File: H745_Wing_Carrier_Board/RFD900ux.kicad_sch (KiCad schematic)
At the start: 1 part

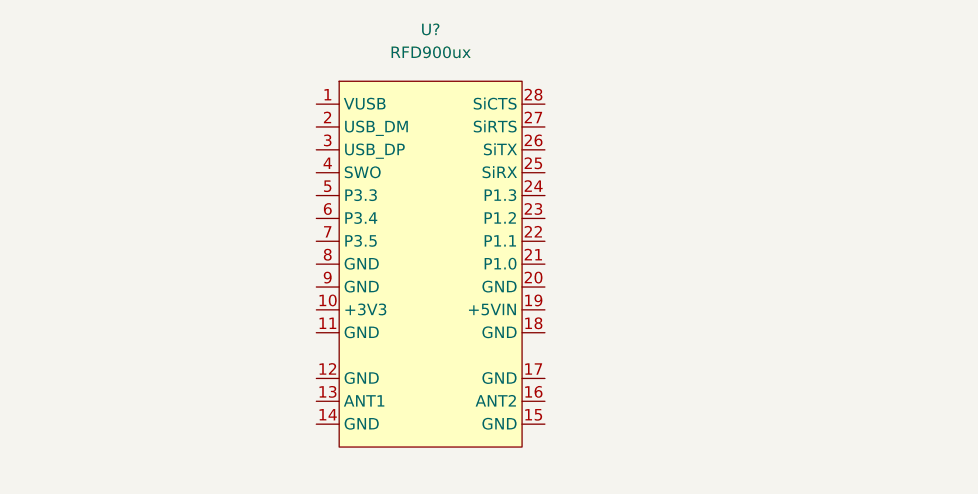
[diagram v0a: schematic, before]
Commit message: Added rfd900ux
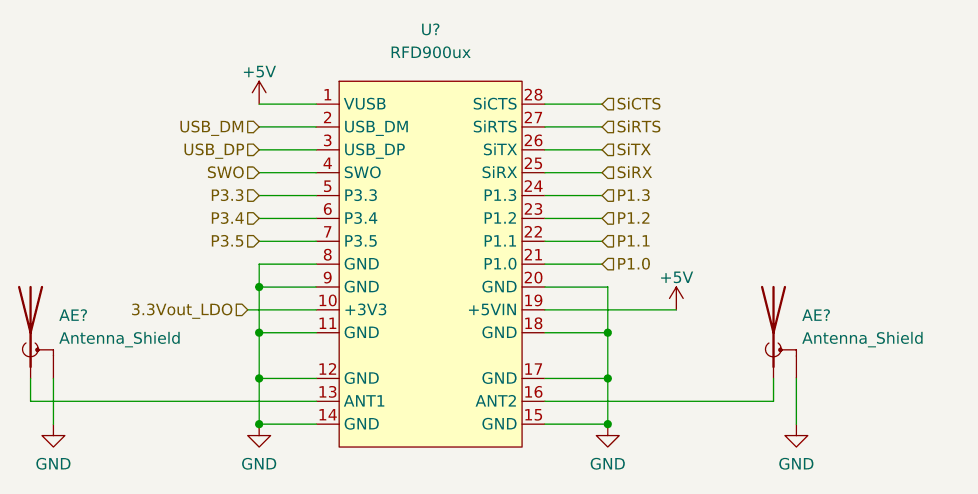
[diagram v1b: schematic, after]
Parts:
- added AE? (x2): Antenna_Shield, symbol Device:Antenna_Shield
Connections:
- net +5V: now reaches U?.1 (VUSB)
- net +5V: now also U?.19 (+5VIN)
- net 3.3Vout_LDO: now reaches U?.10 (+3V3)
- net GND: now reaches U?.11 (GND)
- net GND: now also U?.12 (GND), U?.14 (GND), U?.15 (GND), U?.17 (GND), U?.18 (GND), U?.20 (GND), U?.8 (GND), U?.9 (GND), AE?.2 (Shield), AE?.2 (Shield)
- net at U?.13 (ANT1): now also AE?.1 (A)
- net at U?.16 (ANT2): now also AE?.1 (A)
- net USB_DM: now reaches U?.2 (USB_DM)
- net P1.0: now reaches U?.21 (P1.0)
- net P1.1: now reaches U?.22 (P1.1)
- net P1.2: now reaches U?.23 (P1.2)
- net P1.3: now reaches U?.24 (P1.3)
- net SiRX: now reaches U?.25 (SiRX)
- net SiTX: now reaches U?.26 (SiTX)
- net SiRTS: now reaches U?.27 (SiRTS)
- net SiCTS: now reaches U?.28 (SiCTS)
- net USB_DP: now reaches U?.3 (USB_DP)
- net SWO: now reaches U?.4 (SWO)
- net P3.3: now reaches U?.5 (P3.3)
- net P3.4: now reaches U?.6 (P3.4)
- net P3.5: now reaches U?.7 (P3.5)

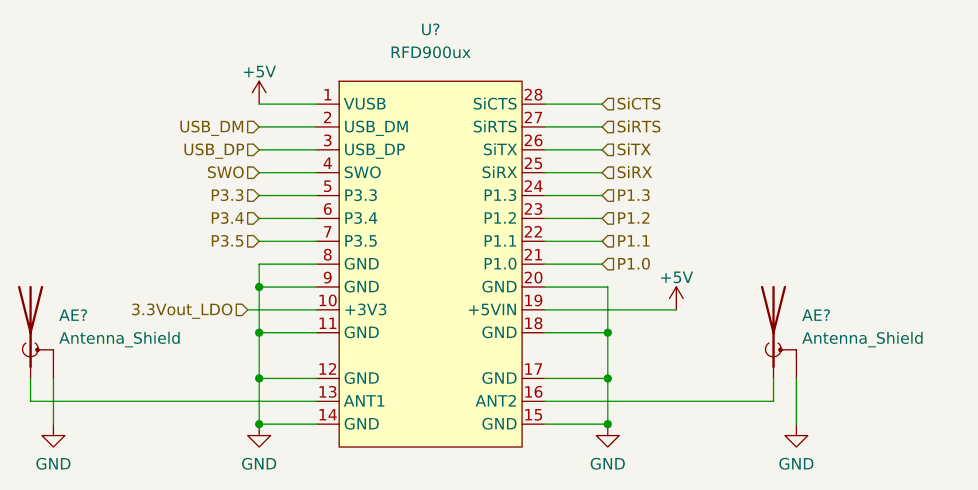
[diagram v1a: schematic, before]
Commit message: Added footprints for ux
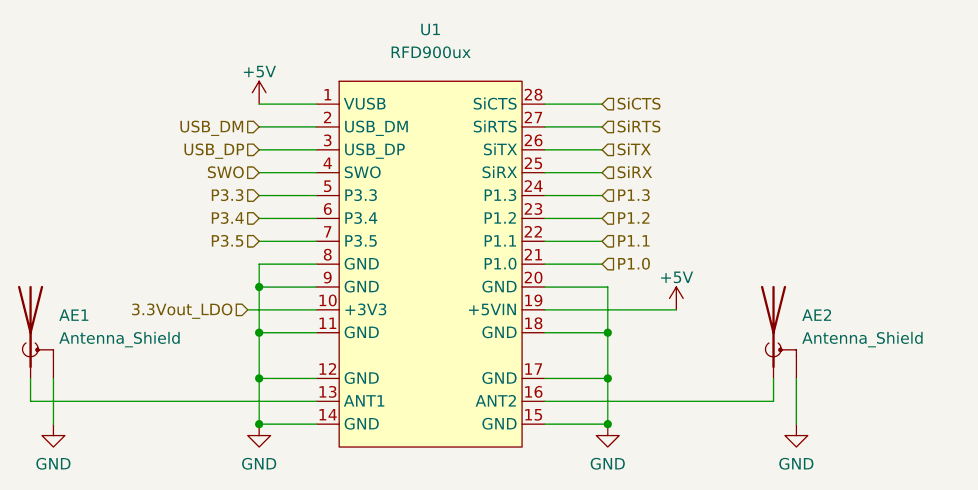
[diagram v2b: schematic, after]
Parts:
- AE1, AE2: renamed from AE?; footprint (none) -> Connector_Coaxial:SMA_Amphenol_132134-16_Vertical
- gave numbers to parts that had none: 1
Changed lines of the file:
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@@
   (symbol (lib_id "power:GND") (at 107.315 111.125 0) (unit 1)
     (in_bom yes) (on_board yes) (fields_autoplaced)
-    (property "Reference" "#PWR?" (id 0) (at 107.315 117.475 0)
+    (property "Reference" "#PWR0108" (id 0) (at 107.315 117.475 0)
       (effects (font (size 1.27 1.27)) hide)
     )
@@
   (symbol (lib_id "power:GND") (at 189.865 111.125 0) (unit 1)
     (in_bom yes) (on_board yes) (fields_autoplaced)
-    (property "Reference" "#PWR?" (id 0) (at 189.865 117.475 0)
+    (property "Reference" "#PWR0110" (id 0) (at 189.865 117.475 0)
       (effects (font (size 1.27 1.27)) hide)
     )
@@
   (symbol (lib_id "Device:Antenna_Shield") (at 104.775 100.965 0) (unit 1)
     (in_bom yes) (on_board yes) (fields_autoplaced)
-    (property "Reference" "AE?" (id 0) (at 107.95 99.0599 0)
+    (property "Reference" "AE1" (id 0) (at 107.95 99.0599 0)
       (effects (font (size 1.27 1.27)) (justify left))
     )
@@
       (effects (font (size 1.27 1.27)) (justify left))
     )
-    (property "Footprint" "" (id 2) (at 104.775 98.425 0)
+    (property "Footprint" "Connector_Coaxial:SMA_Amphenol_132134-16_Vertical" (id 2) (at 104.775 98.425 0)
       (effects (font (size 1.27 1.27)) hide)
     )
@@
   (symbol (lib_id "RFD900ux:RFD900ux") (at 149.225 95.885 0) (unit 1)
     (in_bom yes) (on_board yes) (fields_autoplaced)
-    (property "Reference" "U?" (id 0) (at 149.225 67.31 0))
+    (property "Reference" "U1" (id 0) (at 149.225 67.31 0))
     (property "Value" "RFD900ux" (id 1) (at 149.225 69.85 0))
     (property "Footprint" "Footprints:RFD900ux" (id 2) (at 149.86 72.39 0)
@@
   (symbol (lib_id "power:GND") (at 168.91 111.125 0) (unit 1)
     (in_bom yes) (on_board yes) (fields_autoplaced)
-    (property "Reference" "#PWR?" (id 0) (at 168.91 117.475 0)
+    (property "Reference" "#PWR0111" (id 0) (at 168.91 117.475 0)
       (effects (font (size 1.27 1.27)) hide)
     )
@@
   (symbol (lib_id "power:+5V") (at 130.175 75.565 0) (unit 1)
     (in_bom yes) (on_board yes) (fields_autoplaced)
-    (property "Reference" "#PWR?" (id 0) (at 130.175 79.375 0)
+    (property "Reference" "#PWR0109" (id 0) (at 130.175 79.375 0)
       (effects (font (size 1.27 1.27)) hide)
     )
@@
   (symbol (lib_id "power:+5V") (at 176.53 98.425 0) (unit 1)
     (in_bom yes) (on_board yes) (fields_autoplaced)
-    (property "Reference" "#PWR?" (id 0) (at 176.53 102.235 0)
+    (property "Reference" "#PWR0112" (id 0) (at 176.53 102.235 0)
       (effects (font (size 1.27 1.27)) hide)
     )
@@
   (symbol (lib_id "Device:Antenna_Shield") (at 187.325 100.965 0) (unit 1)
     (in_bom yes) (on_board yes) (fields_autoplaced)
-    (property "Reference" "AE?" (id 0) (at 190.5 99.0599 0)
+    (property "Reference" "AE2" (id 0) (at 190.5 99.0599 0)
       (effects (font (size 1.27 1.27)) (justify left))
     )
@@
       (effects (font (size 1.27 1.27)) (justify left))
     )
-    (property "Footprint" "" (id 2) (at 187.325 98.425 0)
+    (property "Footprint" "Connector_Coaxial:SMA_Amphenol_132134-16_Vertical" (id 2) (at 187.325 98.425 0)
       (effects (font (size 1.27 1.27)) hide)
     )
@@
   (symbol (lib_id "power:GND") (at 130.175 111.125 0) (unit 1)
     (in_bom yes) (on_board yes) (fields_autoplaced)
-    (property "Reference" "#PWR?" (id 0) (at 130.175 117.475 0)
+    (property "Reference" "#PWR0107" (id 0) (at 130.175 117.475 0)
       (effects (font (size 1.27 1.27)) hide)
     )

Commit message: Fixed layout
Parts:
- added J6: USB_B_Micro, Connector_USB:USB_Micro-B_Molex-105017-0001, symbol Connector:USB_B_Micro
- added U8: USBLC6-2SC6, Package_TO_SOT_SMD:SOT-23-6, symbol Power_Protection:USBLC6-2SC6
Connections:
- net GND: now also J6.5 (GND), J6.6 (Shield), U8.2 (GND)
- net ANT2: now reaches AE1.1 (A), U1.13 (ANT1)
- net ANT1: now reaches AE2.1 (A), U1.16 (ANT2)
- net USB_DM renamed USB_D-
- net USB_D-: now also U8.4 (I/O2)
- net USB_DP renamed USB_D+
- net USB_D+: now also U8.6 (I/O1)
- new net USB2_D+: J6.3 (D+), U8.1 (I/O1)
- new net USB2_D-: J6.2 (D-), U8.3 (I/O2)
- new net VBUS: J6.1 (VBUS), U8.5 (VBUS)
- no-connect marks 0 -> 1
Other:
- note added: "To STM32 USB"

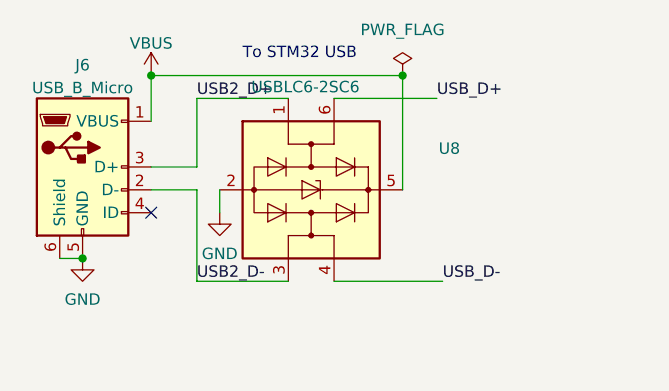
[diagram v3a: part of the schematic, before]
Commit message: Traced together some stuff:
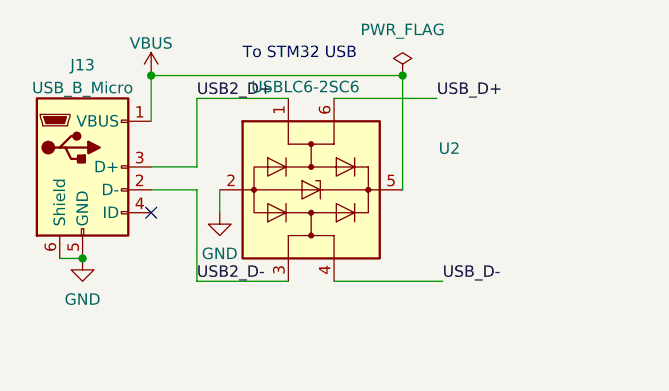
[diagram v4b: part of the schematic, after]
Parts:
- renumbered J6 to J13, U8 to U2
